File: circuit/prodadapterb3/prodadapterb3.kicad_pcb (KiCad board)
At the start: 2 copper layers, 29 x 78 mm, 10 parts, among them J1 Conn_02x20_Odd_Even, J2 Conn_02x05_Odd_Even, J3 Conn_01x02, J4 Conn_02x20_Odd_Even, U1 24LC128

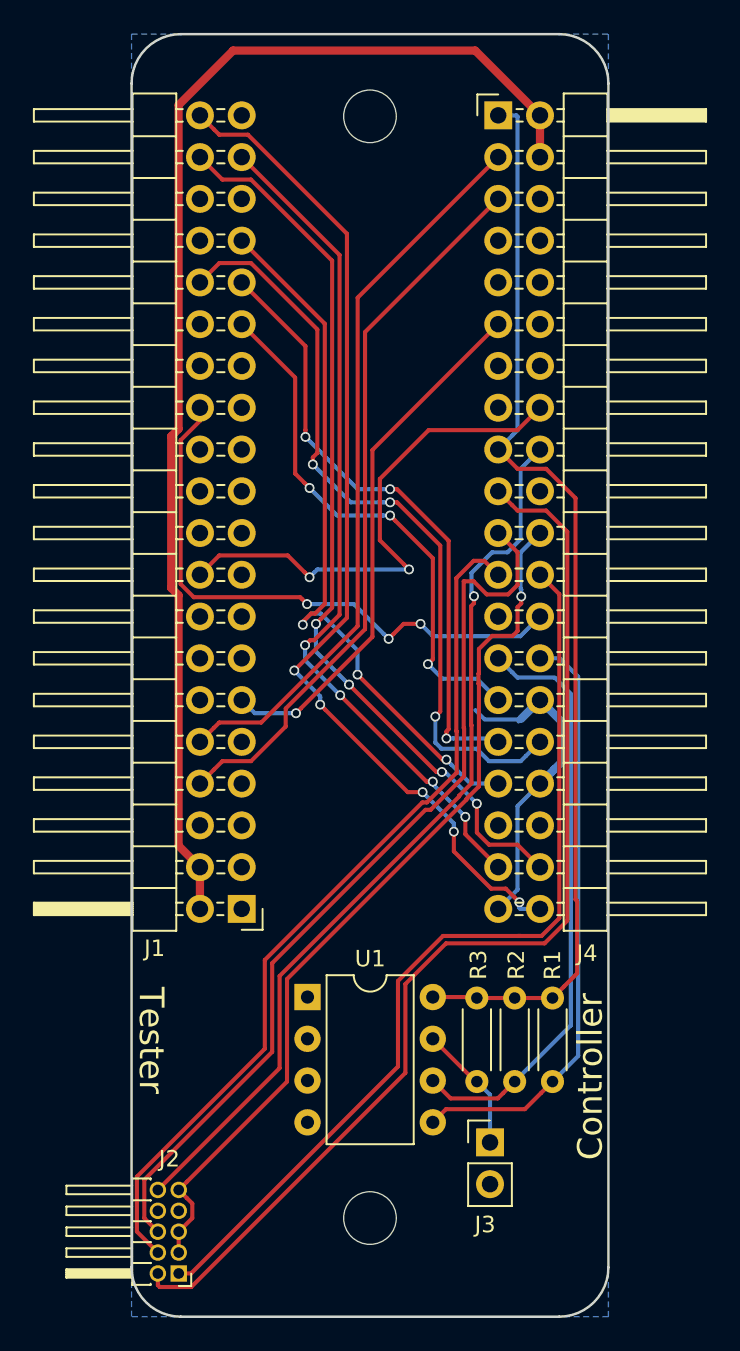
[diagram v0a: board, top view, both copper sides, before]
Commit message: prodadapterb3: move resistors out of the way and connect up 3v3 line
Signed-off-by: Gavan Fantom <gavan.fantom@unipart.io>
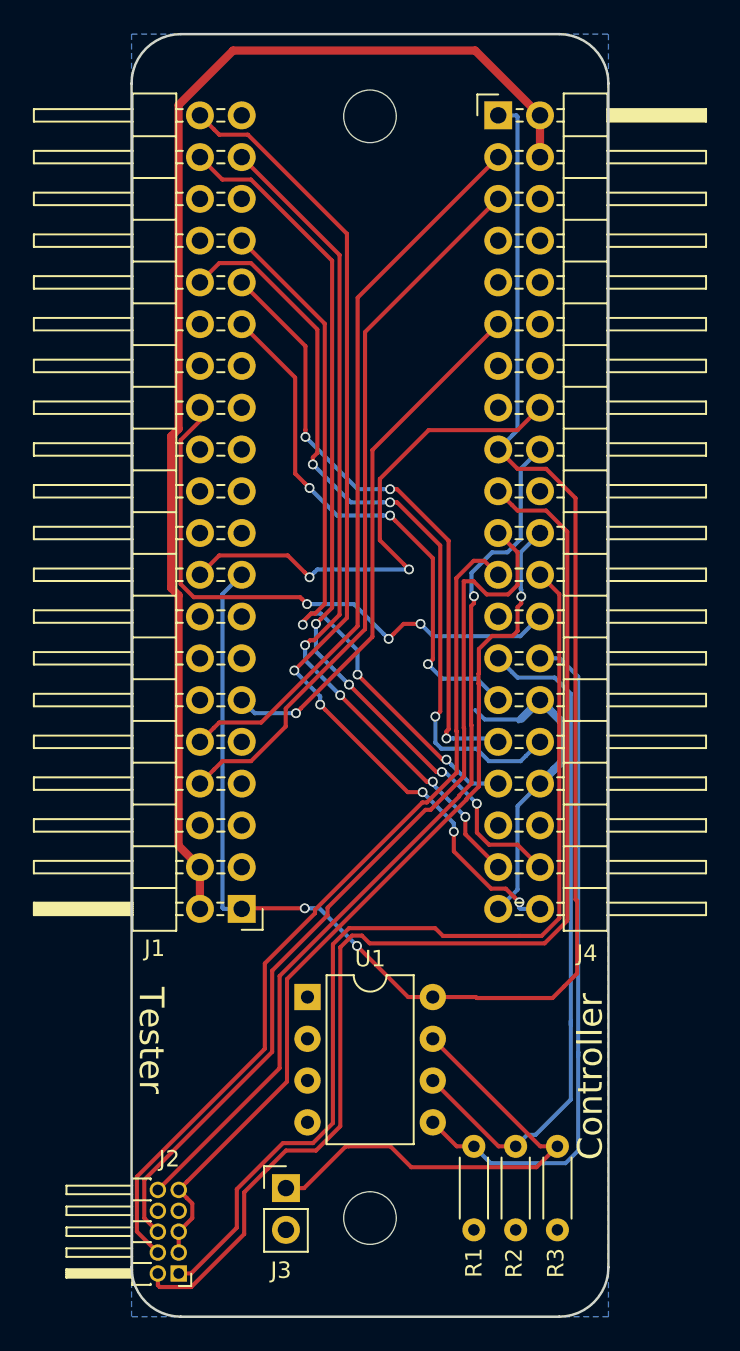
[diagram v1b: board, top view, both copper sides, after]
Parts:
- moved R3 14.9 mm to (152.4, 172.7), turned to 90 degrees
- moved R1 14.9 mm to (147.3, 172.7), turned to 90 degrees
- moved R2 14.1 mm to (149.9, 172.7), turned to 90 degrees
- moved J3 12.7 mm to (135.9, 170.2)
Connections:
- J1 pad 1: Net-(J1-Pad1) -> +3V3
- J1 pad 17: Net-(J1-Pad17) -> +3V3
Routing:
- net +3V3: track 66.2 -> 102.0 mm, vias 0 -> 2
- net Net-(J3-Pad1): track 7.79 -> 28.9 mm
- net Net-(J4-Pad28): track 36.4 -> 42.0 mm
- net Net-(J4-Pad27): track 36.2 -> 41.5 mm
- net PI_MOSI: track 66.9 -> 72.0 mm
- net ~PI_CS: track 56.7 -> 61.8 mm

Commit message: prodadapterb3: Move tester connectors to avoid cable twisting
In order to provide a more straight through approach, the tester
side connectors are placed on the back of the PCB. This allows the
cables to be connected without any twisting, as well as simplifying
the PCB routing.

Signed-off-by: Gavan Fantom <gavan.fantom@unipart.io>
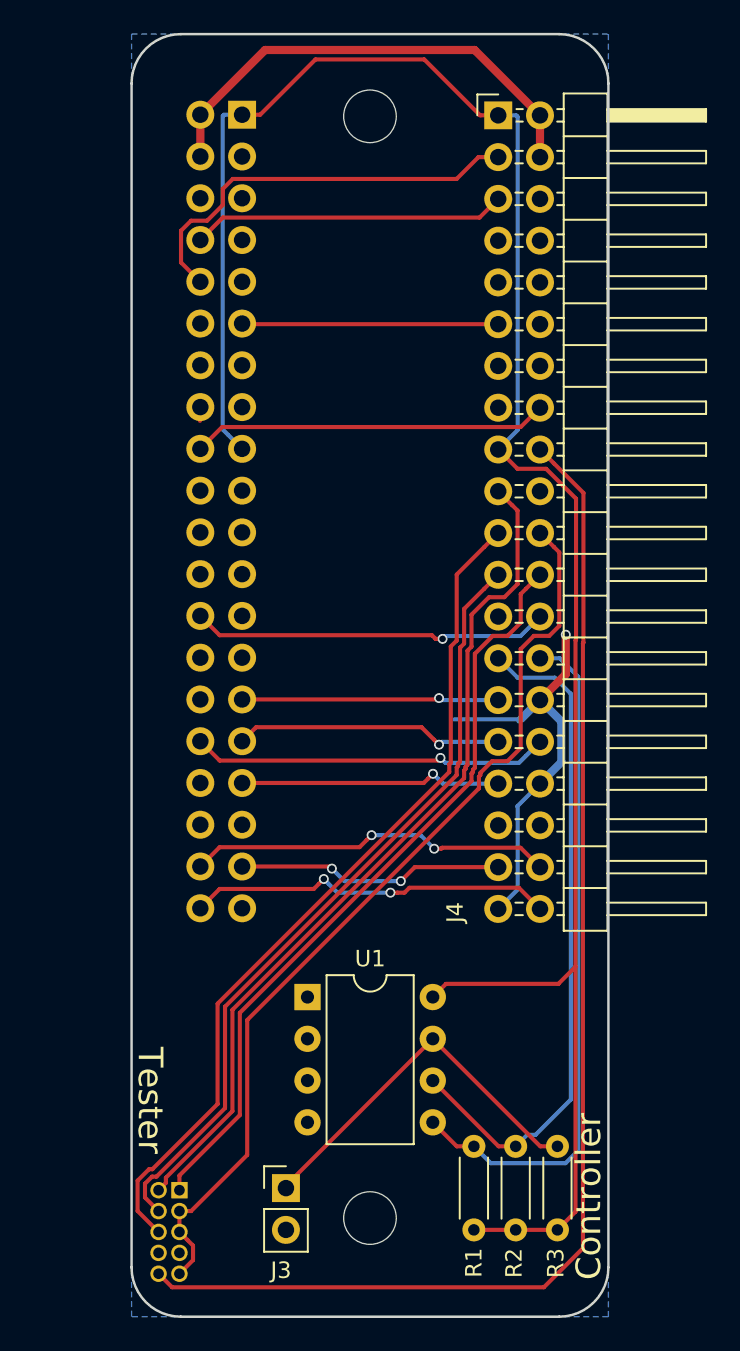
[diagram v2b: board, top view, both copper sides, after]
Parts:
- J1, J2: moved to B.Cu
- moved J1 48.3 mm to (133.2, 104.9)
- moved J2 5.06 mm to (129.4, 170.3)
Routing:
- net +5V: track 77.3 -> 29.0 mm
- net PI_JTAG: track 62.2 -> 22.4 mm, vias 5 -> 2
- net PI_NEG_GROUND: track 51.7 -> 16.3 mm, vias 4 -> 2
- net PI_UART: track 54.9 -> 22.3 mm, vias 4 -> 2
- net PI_MEASURE_LED0: track 43.6 -> 16.1 mm, vias 3 -> 1
- net +3V3: track 102.0 -> 127.7 mm, vias 2 -> 0
- net PI_MEASURE_LED1: track 47.3 -> 22.4 mm, vias 3 -> 1
- net PI_ID_SC: track 44.1 -> 19.2 mm
- net ~PI_RST: track 55.4 -> 76.8 mm, vias 1 -> 0
- net PI_MEASURE_LED2: track 37.6 -> 16.7 mm, vias 3 -> 1
- net PI_MOSI: track 72.0 -> 52.6 mm
- net PI_ID_SD: track 44.6 -> 25.3 mm
- net PI_MEASURE_LED3: track 32.7 -> 15.7 mm, vias 3 -> 1
- net PI_POWER_5V: track 32.4 -> 15.6 mm, vias 1 -> 0
- net ~PI_CS: track 61.8 -> 47.0 mm
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
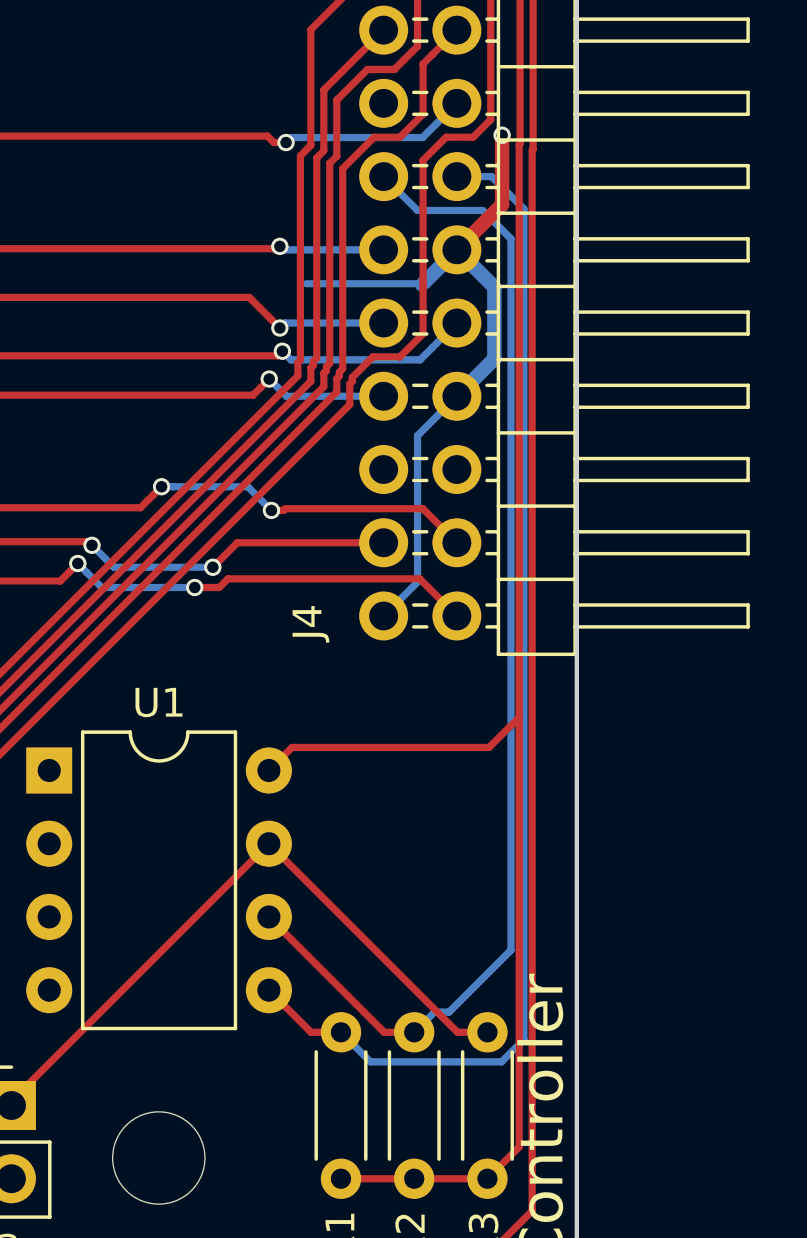
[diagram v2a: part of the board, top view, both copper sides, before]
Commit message: prodadapterb3: Swap SCA and SCL (oops!)
Signed-off-by: Gavan Fantom <gavan.fantom@unipart.io>
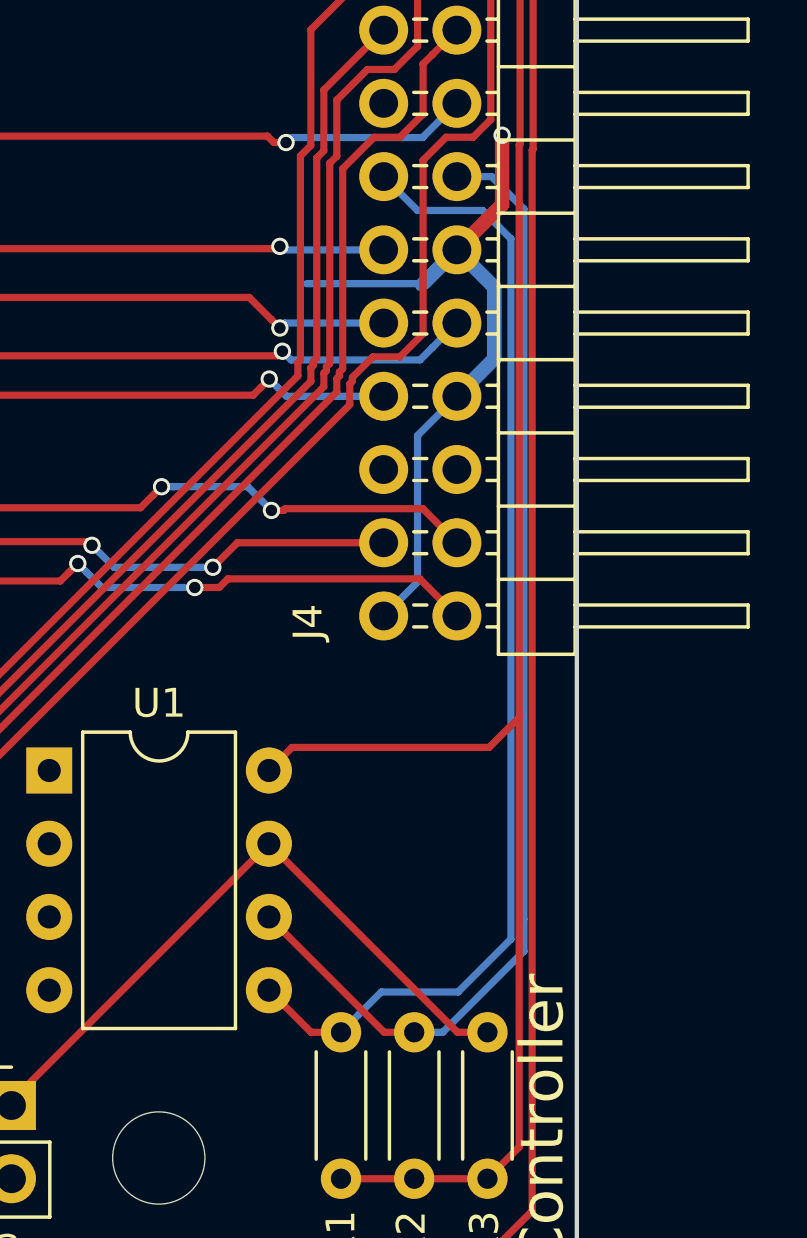
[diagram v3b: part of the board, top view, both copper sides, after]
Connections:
- R1 pad 2: Net-(J4-Pad28) -> Net-(J4-Pad27)
- R2 pad 2: Net-(J4-Pad27) -> Net-(J4-Pad28)
- U1 pad 5: Net-(J4-Pad28) -> Net-(J4-Pad27)
- U1 pad 6: Net-(J4-Pad27) -> Net-(J4-Pad28)
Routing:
- net Net-(J4-Pad28): track 41.8 -> 40.2 mm
- net Net-(J4-Pad27): track 41.2 -> 39.9 mm
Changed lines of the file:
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@@
   (general
     (links 57)
-    (no_connects 0)
+    (no_connects 2)
     (area 126.424999 99.924999 155.575001 178.075001)
     (thickness 1.6)
     (drawings 10)
-    (tracks 253)
+    (tracks 254)
     (zones 0)
     (modules 10)
@@
   )
   (setup
-    (last_trace_width 0.5)
+    (last_trace_width 0.25)
     (user_trace_width 0.5)
     (trace_clearance 0.2)
@@
       (net 39 +3V3))
     (pad 2 thru_hole oval (at 5.08 0 90) (size 1.4 1.4) (drill 0.7) (layers *.Cu *.Mask)
-      (net 47 "Net-(J4-Pad28)"))
+      (net 46 "Net-(J4-Pad27)"))
     (model ${KISYS3DMOD}/Resistors_THT.3dshapes/R_Axial_DIN0204_L3.6mm_D1.6mm_P5.08mm_Horizontal.wrl
       (at (xyz 0 0 0))
@@
       (net 39 +3V3))
     (pad 2 thru_hole oval (at 5.08 0 90) (size 1.4 1.4) (drill 0.7) (layers *.Cu *.Mask)
-      (net 46 "Net-(J4-Pad27)"))
+      (net 47 "Net-(J4-Pad28)"))
     (model ${KISYS3DMOD}/Resistors_THT.3dshapes/R_Axial_DIN0204_L3.6mm_D1.6mm_P5.08mm_Horizontal.wrl
       (at (xyz 0 0 0))
@@
       (net 4 GND))
     (pad 5 thru_hole oval (at 7.62 7.62) (size 1.6 1.6) (drill 0.8) (layers *.Cu *.Mask)
+      (net 46 "Net-(J4-Pad27)"))
+    (pad 2 thru_hole oval (at 0 2.54) (size 1.6 1.6) (drill 0.8) (layers *.Cu *.Mask)
+      (net 4 GND))
+    (pad 6 thru_hole oval (at 7.62 5.08) (size 1.6 1.6) (drill 0.8) (layers *.Cu *.Mask)
       (net 47 "Net-(J4-Pad28)"))
-    (pad 2 thru_hole oval (at 0 2.54) (size 1.6 1.6) (drill 0.8) (layers *.Cu *.Mask)
-      (net 4 GND))
-    (pad 6 thru_hole oval (at 7.62 5.08) (size 1.6 1.6) (drill 0.8) (layers *.Cu *.Mask)
-      (net 46 "Net-(J4-Pad27)"))
     (pad 3 thru_hole oval (at 0 5.08) (size 1.6 1.6) (drill 0.8) (layers *.Cu *.Mask)
       (net 4 GND))
@@
   (segment (start 149.975001 105.015001) (end 149.975001 124.084999) (width 0.25) (layer B.Cu) (net 39))
   (segment (start 149.975001 124.084999) (end 148.8 125.26) (width 0.25) (layer B.Cu) (net 39) (status 20))
-  (segment (start 153.215012 164.792988) (end 153.215012 140.115012) (width 0.25) (layer B.Cu) (net 46))
-  (segment (start 151.067999 166.940001) (end 153.215012 164.792988) (width 0.25) (layer B.Cu) (net 46))
-  (segment (start 149.86 167.64) (end 150.559999 166.940001) (width 0.25) (layer B.Cu) (net 46) (status 10))
-  (segment (start 150.559999 166.940001) (end 151.067999 166.940001) (width 0.25) (layer B.Cu) (net 46))
-  (segment (start 144.82 163.64) (end 148.82 167.64) (width 0.25) (layer F.Cu) (net 46) (status 10))
-  (segment (start 148.82 167.64) (end 149.86 167.64) (width 0.25) (layer F.Cu) (net 46) (status 20))
-  (segment (start 149.975001 139.135001) (end 148.8 137.96) (width 0.25) (layer B.Cu) (net 46) (status 20))
-  (segment (start 152.235001 139.135001) (end 149.975001 139.135001) (width 0.25) (layer B.Cu) (net 46))
-  (segment (start 153.215012 140.115012) (end 152.235001 139.135001) (width 0.25) (layer B.Cu) (net 46))
-  (segment (start 153.665023 167.891979) (end 153.665023 139.082942) (width 0.25) (layer B.Cu) (net 47))
-  (segment (start 147.32 167.64) (end 148.345001 168.665001) (width 0.25) (layer B.Cu) (net 47) (status 10))
-  (segment (start 148.345001 168.665001) (end 152.892001 168.665001) (width 0.25) (layer B.Cu) (net 47))
-  (segment (start 152.892001 168.665001) (end 153.665023 167.891979) (width 0.25) (layer B.Cu) (net 47))
-  (segment (start 144.82 166.18) (end 146.28 167.64) (width 0.25) (layer F.Cu) (net 47) (status 10))
-  (segment (start 146.28 167.64) (end 147.32 167.64) (width 0.25) (layer F.Cu) (net 47) (status 20))
+  (segment (start 148.8 137.96) (end 149.975001 139.135001) (width 0.25) (layer B.Cu) (net 46))
+  (segment (start 149.975001 139.135001) (end 152.235001 139.135001) (width 0.25) (layer B.Cu) (net 46))
+  (segment (start 152.235001 139.135001) (end 153.215012 140.115012) (width 0.25) (layer B.Cu) (net 46))
+  (segment (start 148.717 166.243) (end 147.955 167.005) (width 0.25) (layer B.Cu) (net 46))
+  (segment (start 153.215012 140.115012) (end 153.215012 164.411988) (width 0.25) (layer B.Cu) (net 46))
+  (segment (start 153.215012 164.411988) (end 151.384 166.243) (width 0.25) (layer B.Cu) (net 46))
+  (segment (start 151.384 166.243) (end 148.717 166.243) (width 0.25) (layer B.Cu) (net 46))
+  (segment (start 147.955 167.005) (end 147.32 167.64) (width 0.25) (layer B.Cu) (net 46))
+  (segment (start 144.82 166.18) (end 146.28 167.64) (width 0.25) (layer F.Cu) (net 46) (status 10))
+  (segment (start 146.28 167.64) (end 147.32 167.64) (width 0.25) (layer F.Cu) (net 46) (status 20))
+  (segment (start 153.665023 163.703) (end 153.665023 139.082942) (width 0.25) (layer B.Cu) (net 47))
+  (segment (start 149.86 167.64) (end 150.849949 167.64) (width 0.25) (layer B.Cu) (net 47))
+  (segment (start 150.849949 167.64) (end 153.665023 164.824926) (width 0.25) (layer B.Cu) (net 47))
+  (segment (start 153.665023 164.824926) (end 153.665023 163.703) (width 0.25) (layer B.Cu) (net 47))
   (segment (start 153.665023 139.082942) (end 152.542081 137.96) (width 0.25) (layer B.Cu) (net 47))
+  (segment (start 144.82 163.64) (end 148.82 167.64) (width 0.25) (layer F.Cu) (net 47) (status 10))
+  (segment (start 148.82 167.64) (end 149.86 167.64) (width 0.25) (layer F.Cu) (net 47) (status 20))
   (segment (start 152.542081 137.96) (end 151.34 137.96) (width 0.25) (layer B.Cu) (net 47) (status 20))
   (zone (net 4) (net_name GND) (layer B.Cu) (hatch edge 0.508)
